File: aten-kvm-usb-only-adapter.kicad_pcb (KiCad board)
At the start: 2 copper layers, 31.7 x 20.7 mm, 2 parts, among them J1 DE15_Plug_HighDensity_Mountin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, J2 USB_B

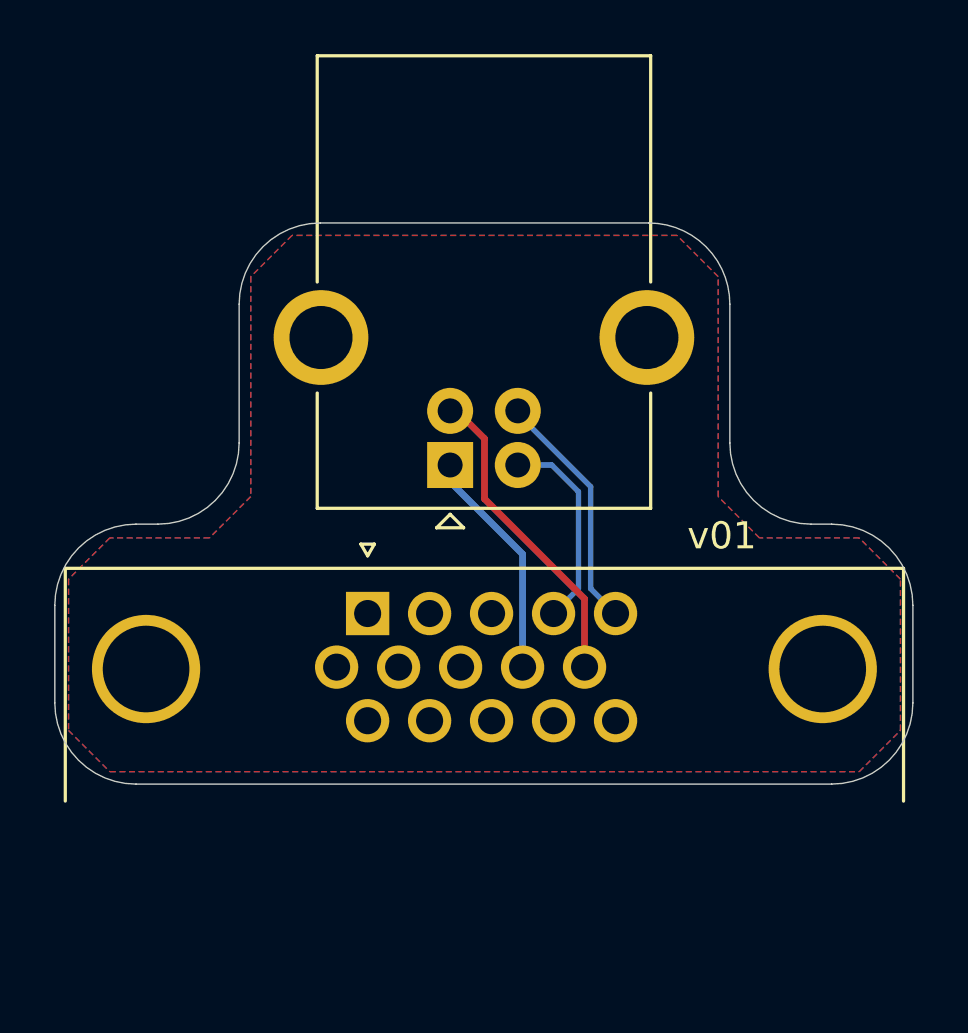
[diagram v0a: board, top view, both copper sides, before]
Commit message: v02: Route GND on the back
This keeps the top as a SHIELD filled layer.
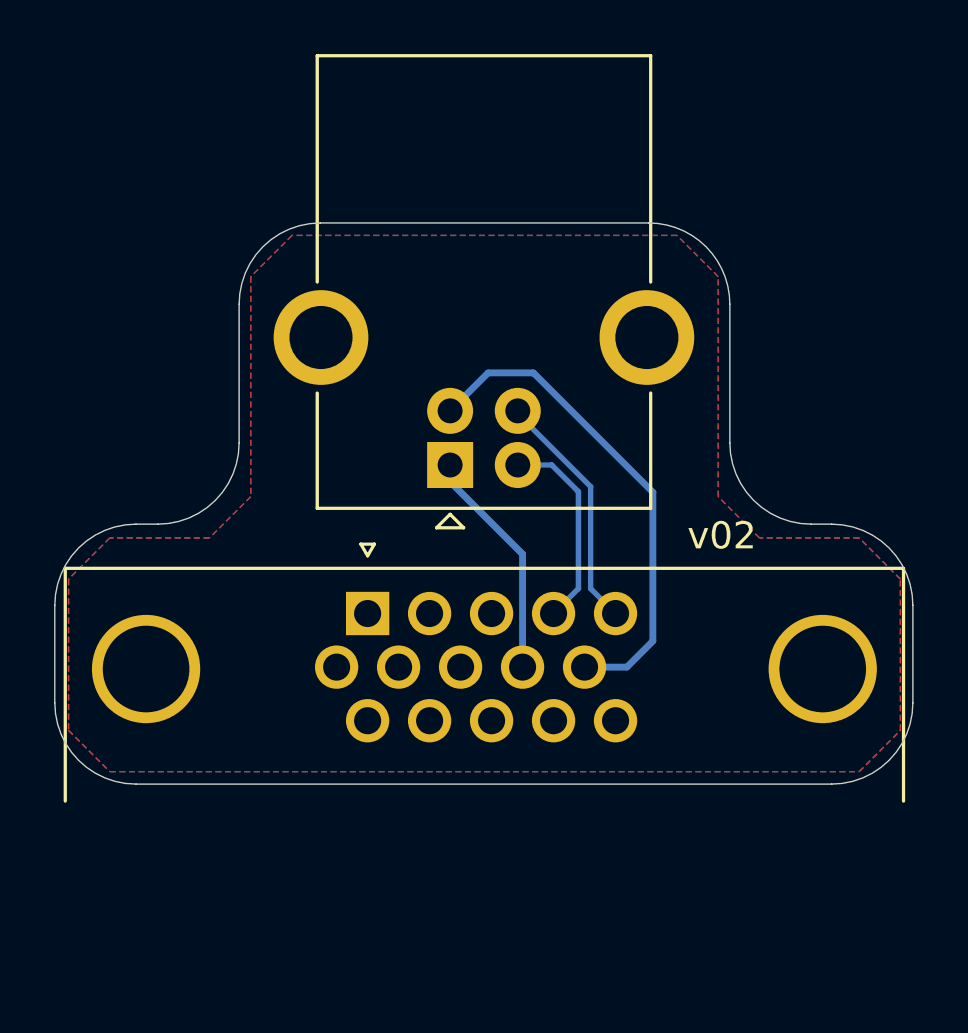
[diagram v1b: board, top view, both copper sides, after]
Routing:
- net GND: track 11.8 -> 18.3 mm
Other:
- board text added: "v02"
- board text removed: "v01"
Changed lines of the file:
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@@
   (gr_line (start 116.88798 86.408) (end 116.88798 81.28)
     (stroke (width 0.05) (type default)) (layer "Edge.Cuts"))
-  (gr_text "v01" (at 115.316 90.424) (layer "F.SilkS")
+  (gr_text "v02" (at 115.316 90.424) (layer "F.SilkS")
     (effects (font (size 1 1) (thickness 0.15)) (justify left bottom))
   )
@@
   (segment (start 106.553 87.8375) (end 109.23 90.5145) (width 0.25) (layer "B.Cu") (net 9))
   (segment (start 109.23 90.5145) (end 109.23 94.69) (width 0.25) (layer "B.Cu") (net 9))
-  (segment (start 111.52 92.168104) (end 111.52 94.69) (width 0.25) (layer "F.Cu") (net 10))
-  (segment (start 106.796 85.2225) (end 107.823 86.2495) (width 0.25) (layer "F.Cu") (net 10))
-  (segment (start 106.446 85.2225) (end 106.796 85.2225) (width 0.25) (layer "F.Cu") (net 10))
-  (segment (start 107.823 86.2495) (end 107.823 88.471104) (width 0.25) (layer "F.Cu") (net 10))
-  (segment (start 107.823 88.471104) (end 111.52 92.168104) (width 0.25) (layer "F.Cu") (net 10))
+  (segment (start 107.9555 83.82) (end 109.63275 83.82) (width 0.25) (layer "B.Cu") (net 10))
+  (segment (start 109.63275 83.82) (end 114.046 88.23325) (width 0.25) (layer "B.Cu") (net 10))
+  (segment (start 114.046 88.23325) (end 114.046 93.726) (width 0.25) (layer "B.Cu") (net 10))
+  (segment (start 114.046 93.726) (end 113.082 94.69) (width 0.25) (layer "B.Cu") (net 10))
+  (segment (start 106.553 85.2225) (end 107.9555 83.82) (width 0.25) (layer "B.Cu") (net 10))
+  (segment (start 113.082 94.69) (end 111.52 94.69) (width 0.25) (layer "B.Cu") (net 10))
   (zone (net 1) (net_name "Earth") (layers "F&B.Cu") (hatch edge 0.5)
     (connect_pads (clearance 0.5))

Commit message: v03: Use own footprint for male HD15 connector with wider pin spacing
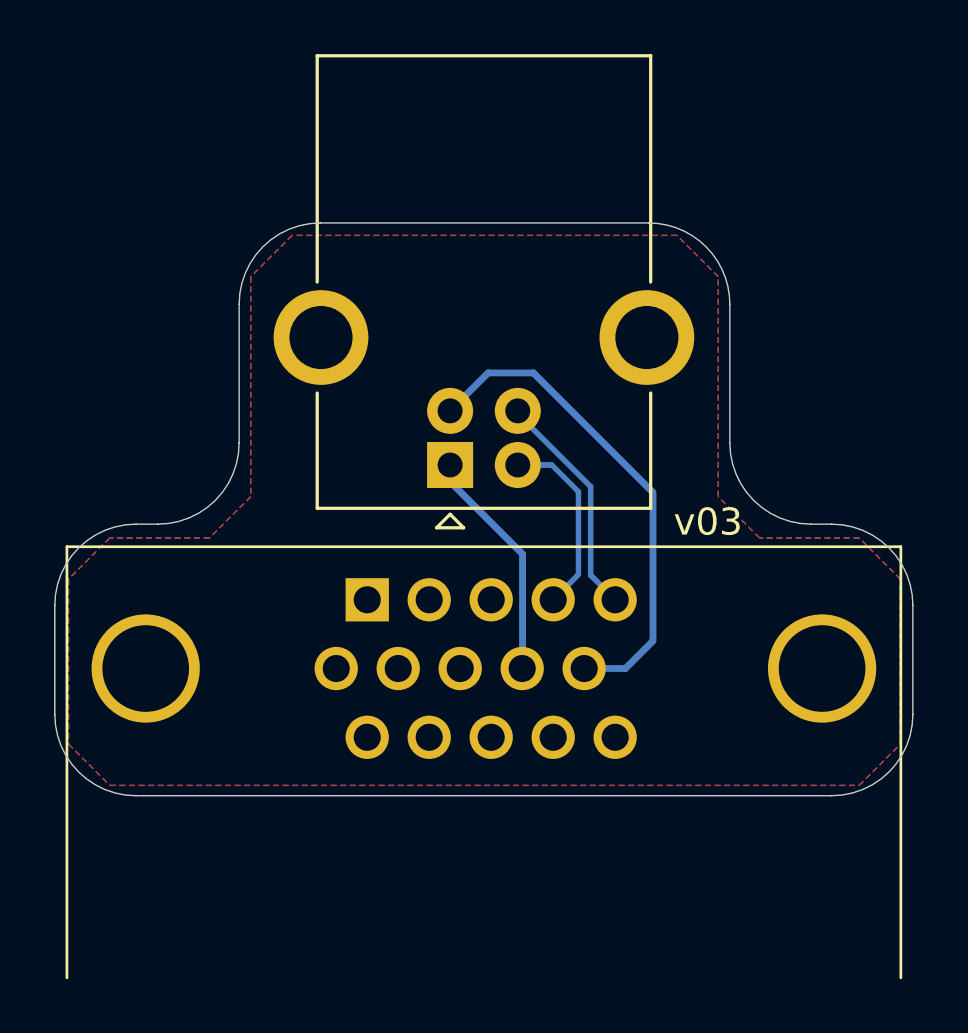
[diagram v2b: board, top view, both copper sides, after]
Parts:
- J1: footprint Connector_Dsub:DSUB-15-HD_Male_Horizontal_P2.29x1.98mm_EdgePinOffset3.03mm_Housed_MountingHolesOffset4.94mm -> own:DSUB-15-HD_Male_Horizontal_Assmann_A-HDS15A-KG-TAXB
- moved J1 4.75 mm to (107.8, 94.7)
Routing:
- net D+: track 8.98 -> 8.47 mm
- net D-: track 7.53 -> 7.03 mm
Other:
- board size 31.7 x 20.7 mm -> 31.7 x 21.2 mm
- board text added: "v03"
- board text removed: "v02"
